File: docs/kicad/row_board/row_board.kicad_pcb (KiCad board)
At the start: 2 copper layers, 200 x 25 mm, 21 parts, among them J1 Conn_01x06, J2 Conn_01x06, SW1 SW1, SW2 SW1, SW3 SW1, SW4 SW1, SW5 SW1, U1 74HC595

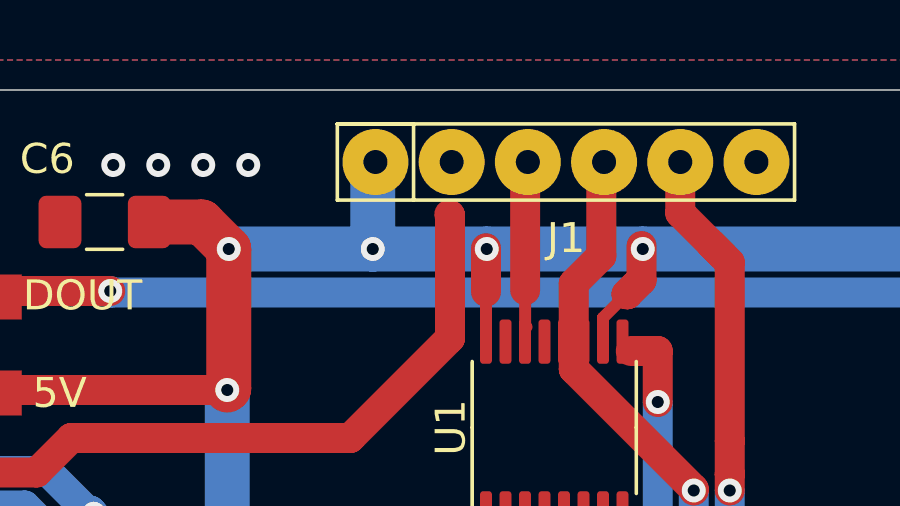
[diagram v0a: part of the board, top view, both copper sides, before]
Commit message: got rid of (many) vestigial TE3 design attempts; consolidating electronics under TE3/docs/kicad
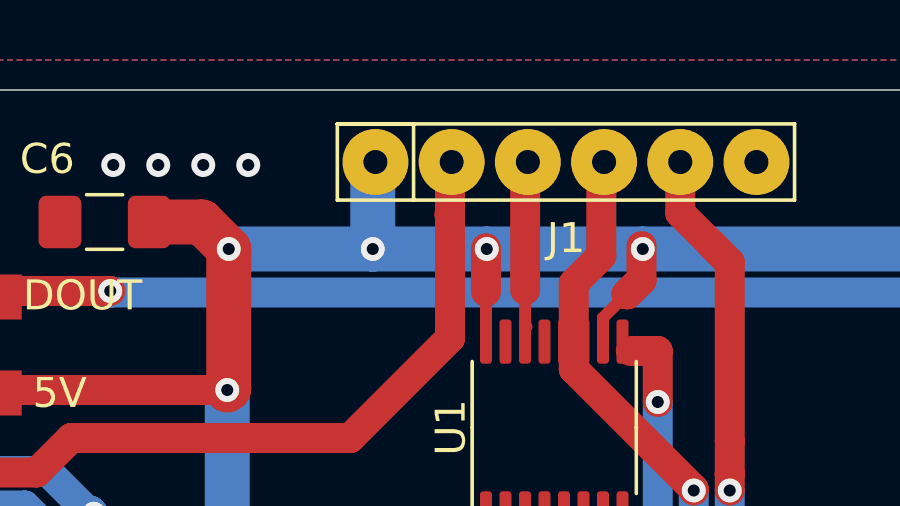
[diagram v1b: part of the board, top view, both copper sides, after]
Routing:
- net DIN: track 123.1 -> 124.8 mm
